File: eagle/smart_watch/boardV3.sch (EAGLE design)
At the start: 51 parts, among them U1 MCP73831, U2 TPS61200, U3 MAX1704X, U4 V_REG_LDOSMD, Y1 16MHz

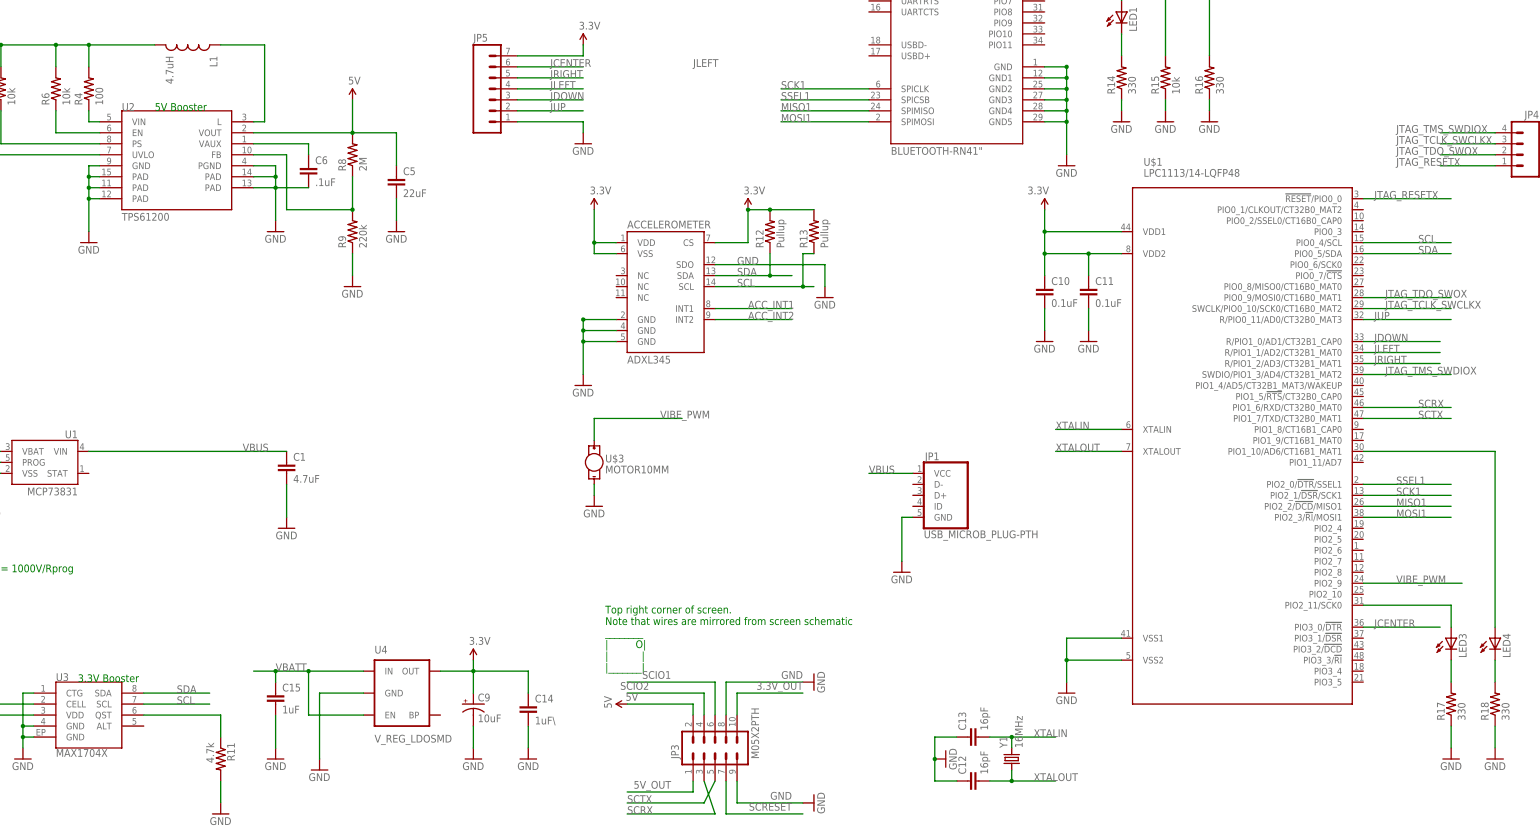
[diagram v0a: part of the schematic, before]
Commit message: Finished off V3 board design. Added silk to boards
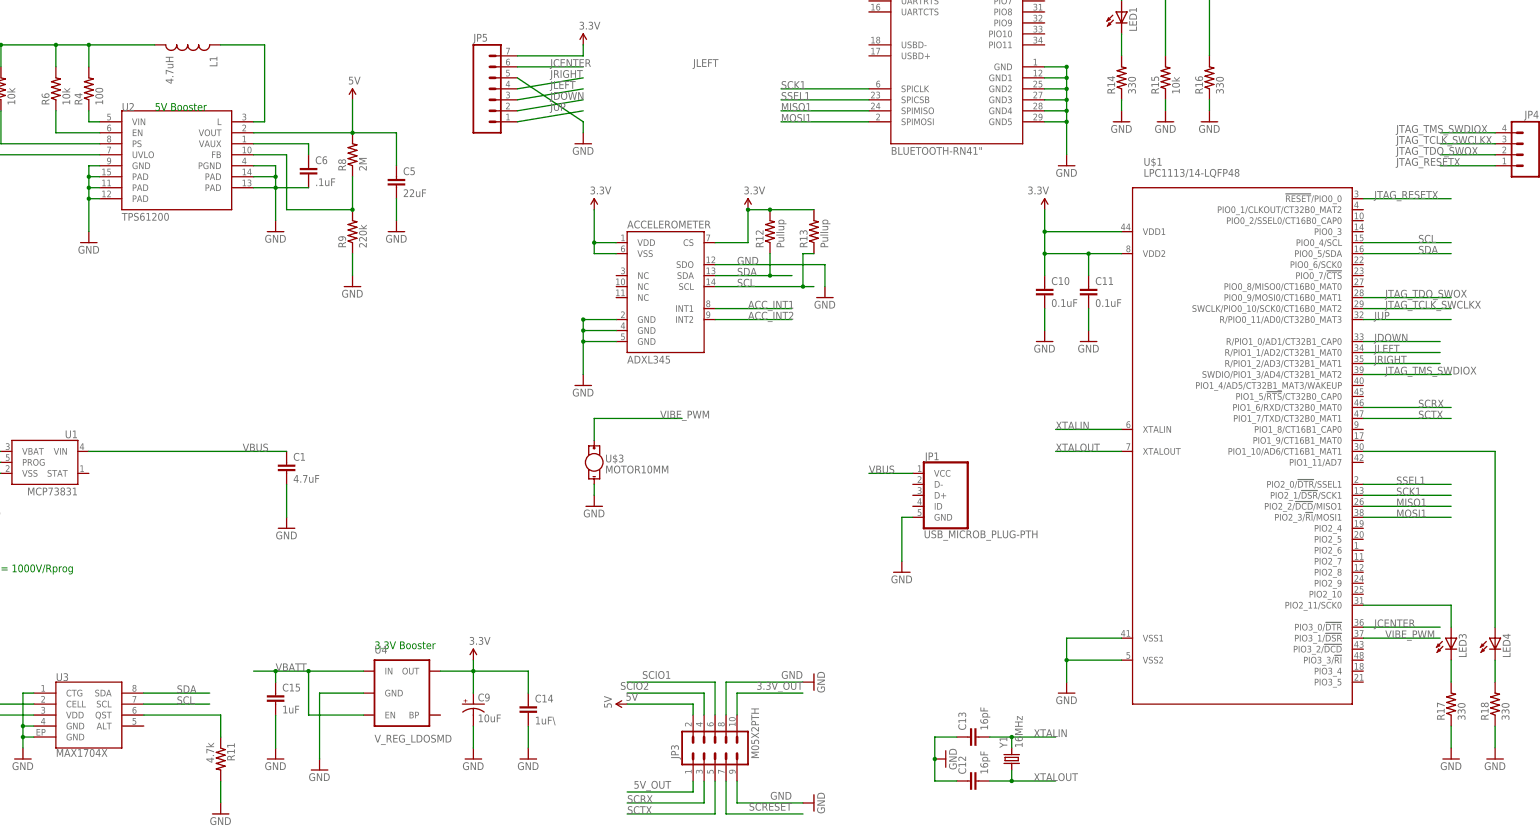
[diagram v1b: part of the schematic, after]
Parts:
- R8, R9: device SparkFun-Passives:RESISTOR0402-RES -> SparkFun-Resistors:RESISTOR0603-RES
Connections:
- net GND: now also JP5.5; no longer JP5.1
- net JDOWN: now also JP5.2; no longer JP5.3
- net JLEFT: now also JP5.3; no longer JP5.4
- net JRIGHT: now also JP5.4; no longer JP5.5
- net JUP: now also JP5.1; no longer JP5.2
- net VIBE_PWM: now also U$1.PIO3_1/!DSR!; no longer U$1.PIO2_9
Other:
- note removed: "Top right corner of screen. Note that wires are mirrored from screen schematic ________ | O| | | |_______|"
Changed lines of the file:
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@@
 <setting verticaltext="up"/>
 </settings>
-<grid distance="0.1" unitdist="inch" unit="inch" style="lines" multiple="1" display="no" altdistance="0.01" altunitdist="inch" altunit="inch"/>
+<grid distance="0.1" unitdist="inch" unit="inch" style="lines" multiple="1" display="yes" altdistance="0.01" altunitdist="inch" altunit="inch"/>
 <layers>
 <layer number="1" name="Top" color="4" fill="1" visible="no" active="no"/>
@@
 <part name="C4" library="SparkFun-Passives" deviceset="CAP" device="0603-CAP" value="10uF"/>
 <part name="R7" library="SparkFun-Passives" deviceset="RESISTOR" device="0603-RES" value="220k"/>
-<part name="R8" library="SparkFun-Passives" deviceset="RESISTOR" device="0402-RES" value="2M"/>
-<part name="R9" library="SparkFun-Passives" deviceset="RESISTOR" device="0402-RES" value="220k"/>
+<part name="R8" library="SparkFun-Resistors" deviceset="RESISTOR" device="0603-RES" value="2M"/>
+<part name="R9" library="SparkFun-Resistors" deviceset="RESISTOR" device="0603-RES" value="220k"/>
 <part name="C5" library="SparkFun-Passives" deviceset="CAP" device="0603-CAP" value="22uF"/>
 <part name="GND10" library="SparkFun-Aesthetics" deviceset="GND" device=""/>
@@
 <text x="-96.52" y="66.04" size="1.778" layer="91">Battery Connector</text>
 <text x="12.7" y="139.7" size="1.778" layer="91">5V Booster</text>
-<text x="-5.08" y="7.62" size="1.778" layer="91">3.3V Booster</text>
-<text x="116.84" y="10.16" size="1.778" layer="91">Top right corner of screen.
-Note that wires are mirrored from screen schematic
-________
-|         O|
-|           |
-|_______|</text>
+<text x="63.5" y="15.24" size="1.778" layer="91">3.3V Booster</text>
 </plain>
 <instances>
@@
 </segment>
 <segment>
-<wire x1="96.52" y1="137.16" x2="111.76" y2="137.16" width="0.2032" layer="91"/>
+<wire x1="96.52" y1="147.32" x2="111.76" y2="137.16" width="0.2032" layer="91"/>
 <wire x1="111.76" y1="137.16" x2="111.76" y2="134.62" width="0.2032" layer="91"/>
 <pinref part="GND34" gate="1" pin="GND"/>
-<pinref part="JP5" gate="G$1" pin="1"/>
+<pinref part="JP5" gate="G$1" pin="5"/>
 </segment>
 <segment>
@@
 <segment>
 <pinref part="JP3" gate="G$1" pin="5"/>
-<wire x1="142.24" y1="-15.24" x2="139.7" y2="-20.32" width="0.2032" layer="91"/>
-<wire x1="139.7" y1="-20.32" x2="121.92" y2="-20.32" width="0.2032" layer="91"/>
-<label x="121.92" y="-20.32" size="1.778" layer="95"/>
+<wire x1="142.24" y1="-15.24" x2="142.24" y2="-22.86" width="0.2032" layer="91"/>
+<wire x1="142.24" y1="-22.86" x2="121.92" y2="-22.86" width="0.2032" layer="91"/>
+<label x="121.92" y="-22.86" size="1.778" layer="95"/>
 </segment>
 <segment>
@@
 <segment>
 <pinref part="JP3" gate="G$1" pin="3"/>
-<wire x1="139.7" y1="-15.24" x2="142.24" y2="-22.86" width="0.2032" layer="91"/>
-<wire x1="142.24" y1="-22.86" x2="121.92" y2="-22.86" width="0.2032" layer="91"/>
-<label x="121.92" y="-22.86" size="1.778" layer="95"/>
+<wire x1="139.7" y1="-15.24" x2="139.7" y2="-20.32" width="0.2032" layer="91"/>
+<wire x1="139.7" y1="-20.32" x2="121.92" y2="-20.32" width="0.2032" layer="91"/>
+<label x="121.92" y="-20.32" size="1.778" layer="95"/>
 </segment>
 <segment>
@@
 <net name="VIBE_PWM" class="0">
 <segment>
-<wire x1="292.1" y1="30.48" x2="314.96" y2="30.48" width="0.2032" layer="91"/>
-<pinref part="U$1" gate="LPC" pin="PIO2_9"/>
-<label x="299.72" y="30.48" size="1.778" layer="95"/>
-</segment>
-<segment>
 <pinref part="U$3" gate="G$1" pin="+"/>
 <wire x1="114.3" y1="63.5" x2="114.3" y2="68.58" width="0.2032" layer="91"/>
 <wire x1="114.3" y1="68.58" x2="134.62" y2="68.58" width="0.2032" layer="91"/>
 <label x="129.54" y="68.58" size="1.778" layer="95"/>
+</segment>
+<segment>
+<pinref part="U$1" gate="LPC" pin="PIO3_1/!DSR!"/>
+<wire x1="292.1" y1="17.78" x2="309.88" y2="17.78" width="0.1524" layer="91"/>
+<label x="297.18" y="17.78" size="1.778" layer="95"/>
 </segment>
 </net>
@@
 </segment>
 <segment>
-<wire x1="96.52" y1="139.7" x2="111.76" y2="139.7" width="0.2032" layer="91"/>
+<wire x1="96.52" y1="137.16" x2="111.76" y2="139.7" width="0.2032" layer="91"/>
 <label x="104.14" y="139.7" size="1.778" layer="95"/>
-<pinref part="JP5" gate="G$1" pin="2"/>
+<pinref part="JP5" gate="G$1" pin="1"/>
 </segment>
 </net>
@@
 </segment>
 <segment>
-<wire x1="96.52" y1="142.24" x2="111.76" y2="142.24" width="0.2032" layer="91"/>
+<wire x1="96.52" y1="139.7" x2="111.76" y2="142.24" width="0.2032" layer="91"/>
 <label x="104.14" y="142.24" size="1.778" layer="95"/>
-<pinref part="JP5" gate="G$1" pin="3"/>
+<pinref part="JP5" gate="G$1" pin="2"/>
 </segment>
 </net>
@@
 </segment>
 <segment>
-<wire x1="96.52" y1="147.32" x2="111.76" y2="147.32" width="0.2032" layer="91"/>
+<wire x1="96.52" y1="144.78" x2="111.76" y2="147.32" width="0.2032" layer="91"/>
 <label x="104.14" y="147.32" size="1.778" layer="95"/>
-<pinref part="JP5" gate="G$1" pin="5"/>
+<pinref part="JP5" gate="G$1" pin="4"/>
 </segment>
 </net>
@@
 <segment>
 <label x="137.16" y="149.86" size="1.778" layer="95"/>
-<wire x1="96.52" y1="144.78" x2="111.76" y2="144.78" width="0.2032" layer="91"/>
+<wire x1="96.52" y1="142.24" x2="111.76" y2="144.78" width="0.2032" layer="91"/>
 <label x="104.14" y="144.78" size="1.778" layer="95"/>
-<pinref part="JP5" gate="G$1" pin="4"/>
-</segment>
-</net>
+<pinref part="JP5" gate="G$1" pin="3"/>
+</segment>
+</net>

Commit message: Board and schema going out for review
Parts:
- added I2C: (no value), SparkFun-Connectors:M02POGO_PIN_HOLES_ONLY
- added JP6: (no value), SparkFun-Connectors:M07
- added LED5: (no value), SparkFun-LED:LED0603
- added R1, R19, R20, R21, R22: 10k, SparkFun-Resistors:RESISTOR0603-RES
- added R23: 330, SparkFun-Passives:RESISTOR0603-RES
- added S1: (no value), SparkFun-Electromechanical:JOYSTICK_MINI
- added SPI: (no value), SparkFun-Connectors:M04POLAR
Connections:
- new net N$21: LED5.C, R23.2
- net 3.3V: now also JP6.7, LED5.A, R1.1, R19.1, R20.1, R21.1, R22.1
- net GND: now also JP6.5, R23.1, S1.GND
- net JCENTER: now also JP5.2, JP6.2, R22.2, S1.CENT, U$1.R/PIO1_0/AD1/CT32B1_CAP0; no longer JP5.6, U$1.PIO3_0/!DTR!
- net JDOWN: now also JP5.4, JP6.4, R1.2, S1.DOWN, U$1.R/PIO1_2/AD3/CT32B1_MAT1; no longer JP5.2, U$1.R/PIO1_0/AD1/CT32B1_CAP0
- net JLEFT: now also JP5.1, JP6.1, R20.2, S1.LEFT, U$1.R/PIO0_11/AD0/CT32B0_MAT3; no longer JP5.3, U$1.R/PIO1_1/AD2/CT32B1_MAT0
- net JRIGHT: now also JP5.6, JP6.6, R21.2, S1.RIGHT, U$1.PIO3_0/!DTR!; no longer JP5.4, U$1.R/PIO1_2/AD3/CT32B1_MAT1
- net JUP: now also JP5.3, JP6.3, R19.2, S1.UP, U$1.R/PIO1_1/AD2/CT32B1_MAT0; no longer JP5.1, U$1.R/PIO0_11/AD0/CT32B0_MAT3
- net MISO1: now also SPI.2
- net MOSI1: now also SPI.1
- net SCK1: now also SPI.4
- net SCL: now also I2C.2
- net SDA: now also I2C.1
- net SSEL1: now also SPI.3

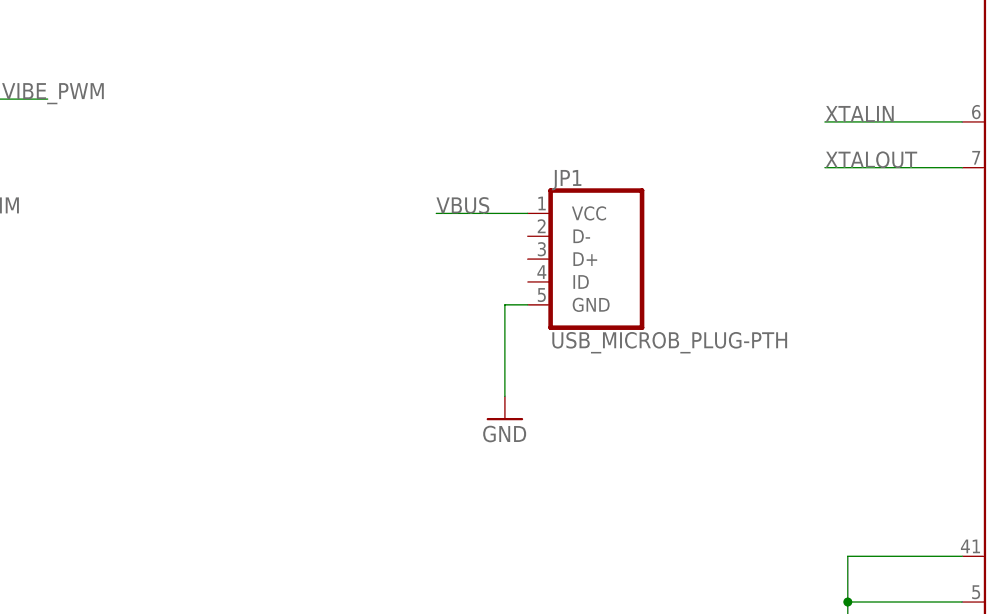
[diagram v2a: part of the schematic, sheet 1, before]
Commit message: Updated usb port and changed some res sizes
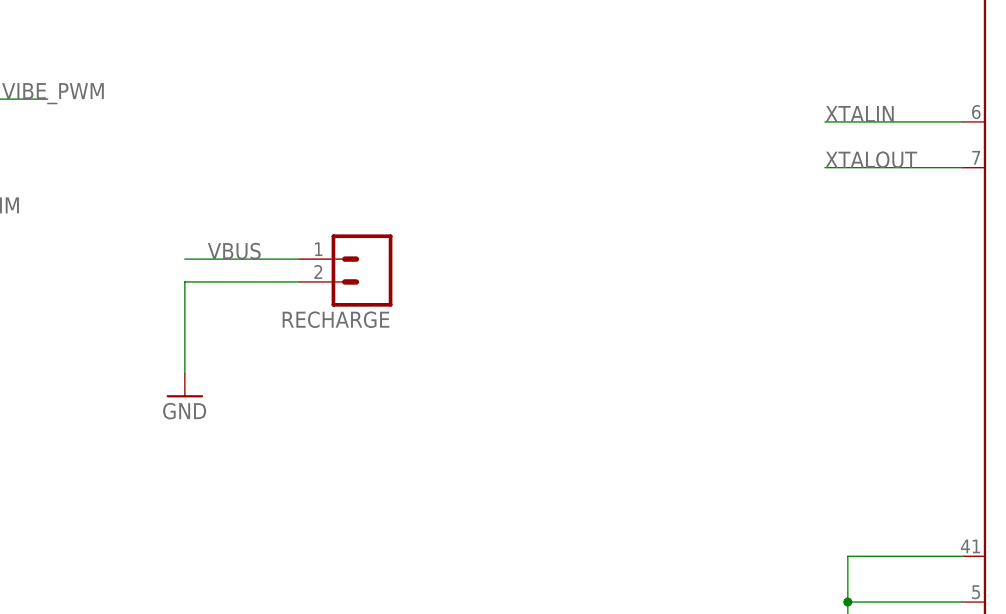
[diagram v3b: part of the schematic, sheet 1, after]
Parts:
- removed JP1: USB_MICROB_PLUG-PTH, SparkFun-Connectors:USB_MICROB_PLUG-PTH
- added RECHARGE: (no value), SparkFun-Connectors:M02POGO_PIN_HOLES_ONLY
- R12, R13: device SparkFun-Passives:RESISTOR0402-RES -> SparkFun-Resistors:RESISTOR0603-RES
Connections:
- net GND: now also RECHARGE.2; no longer JP1.GND
- net VBUS: now also RECHARGE.1; no longer JP1.VCC
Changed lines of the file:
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@@
 <parts>
 <part name="U$1" library="lpc1100v1.1" deviceset="LPC1113/14-LQFP48" device=""/>
-<part name="JP1" library="SparkFun-Connectors" deviceset="USB_MICROB_PLUG" device="-PTH"/>
 <part name="U1" library="SparkFun-PowerIC" deviceset="MCP73831" device=""/>
 <part name="JP2" library="SparkFun-Connectors" deviceset="M02" device="-JST-2-PTH-NO_SILK"/>
-<part name="GND1" library="SparkFun-Aesthetics" deviceset="GND" device=""/>
 <part name="C1" library="SparkFun-Passives" deviceset="CAP" device="0603-CAP" value="4.7uF"/>
 <part name="GND2" library="SparkFun-Aesthetics" deviceset="GND" device=""/>
@@
 <part name="GND29" library="SparkFun-Aesthetics" deviceset="GND" device=""/>
 <part name="SUPPLY8" library="SparkFun-Aesthetics" deviceset="3.3V" device=""/>
-<part name="R12" library="SparkFun-Passives" deviceset="RESISTOR" device="0402-RES" value="Pullup"/>
-<part name="R13" library="SparkFun-Passives" deviceset="RESISTOR" device="0402-RES" value="Pullup"/>
+<part name="R12" library="SparkFun-Resistors" deviceset="RESISTOR" device="0603-RES" value="Pullup"/>
+<part name="R13" library="SparkFun-Resistors" deviceset="RESISTOR" device="0603-RES" value="Pullup"/>
 <part name="Y1" library="SparkFun-FreqCtrl" deviceset="CRYSTAL" device="5X3" value="16MHz"/>
 <part name="C12" library="SparkFun-Passives" deviceset="CAP" device="0603-CAP" value="16pF"/>
@@
 <part name="GND39" library="SparkFun-Aesthetics" deviceset="GND" device=""/>
 <part name="SUPPLY12" library="SparkFun-Aesthetics" deviceset="3.3V" device=""/>
+<part name="RECHARGE" library="SparkFun-Connectors" deviceset="M02" device="POGO_PIN_HOLES_ONLY"/>
+<part name="GND40" library="SparkFun-Aesthetics" deviceset="GND" device=""/>
 </parts>
 <sheets>
@@
 <instances>
 <instance part="U$1" gate="LPC" x="264.16" y="63.5"/>
-<instance part="JP1" gate="G$1" x="195.58" y="50.8"/>
 <instance part="U1" gate="G$1" x="-12.7" y="58.42" rot="MR0"/>
 <instance part="JP2" gate="G$1" x="-88.9" y="58.42"/>
-<instance part="GND1" gate="1" x="185.42" y="33.02"/>
 <instance part="C1" gate="G$1" x="43.18" y="55.88"/>
 <instance part="GND2" gate="1" x="43.18" y="43.18"/>
@@
 <instance part="GND39" gate="1" x="353.06" y="-7.62"/>
 <instance part="SUPPLY12" gate="G$1" x="353.06" y="40.64" rot="MR0"/>
+<instance part="RECHARGE" gate="G$1" x="170.18" y="50.8" rot="R180"/>
+<instance part="GND40" gate="1" x="149.86" y="35.56"/>
 </instances>
 <busses>
@@
 <nets>
 <net name="GND" class="0">
-<segment>
-<pinref part="JP1" gate="G$1" pin="GND"/>
-<pinref part="GND1" gate="1" pin="GND"/>
-<wire x1="187.96" y1="45.72" x2="185.42" y2="45.72" width="0.1524" layer="91"/>
-<wire x1="185.42" y1="45.72" x2="185.42" y2="35.56" width="0.1524" layer="91"/>
-</segment>
 <segment>
 <pinref part="C1" gate="G$1" pin="2"/>
@@
 <pinref part="R23" gate="G$1" pin="1"/>
 <pinref part="GND39" gate="1" pin="GND"/>
+</segment>
+<segment>
+<pinref part="RECHARGE" gate="G$1" pin="2"/>
+<wire x1="162.56" y1="48.26" x2="149.86" y2="48.26" width="0.1524" layer="91"/>
+<wire x1="149.86" y1="48.26" x2="149.86" y2="38.1" width="0.1524" layer="91"/>
+<pinref part="GND40" gate="1" pin="GND"/>
 </segment>
 </net>
@@
 </segment>
 <segment>
-<pinref part="JP1" gate="G$1" pin="VCC"/>
-<wire x1="187.96" y1="55.88" x2="177.8" y2="55.88" width="0.2032" layer="91"/>
-<label x="177.8" y="55.88" size="1.778" layer="95"/>
-</segment>
-</net>
+<pinref part="RECHARGE" gate="G$1" pin="1"/>
+<wire x1="162.56" y1="50.8" x2="149.86" y2="50.8" width="0.1524" layer="91"/>
+<label x="152.4" y="50.8" size="1.778" layer="95"/>
+</segment>
+</net>
